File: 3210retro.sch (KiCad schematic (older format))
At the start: 25 parts, among them P101 USB_OTG, P103 LIPO, P104 DC, P106 SPEAKER, P107 HEADPHONE, P108 RUMBLE, X101 ANT_GPS, X102 ANT_GSM

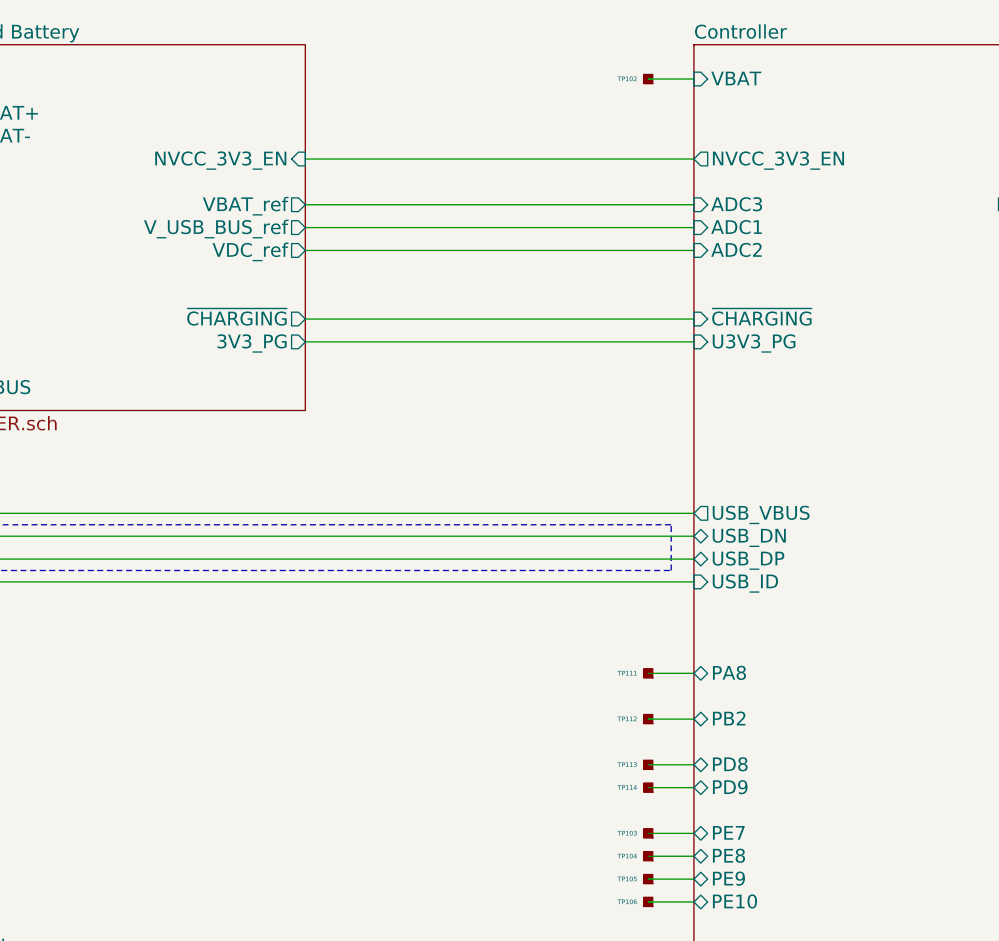
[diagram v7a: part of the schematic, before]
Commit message: finalized borad further
placed more GND vias
make 4V_BST switchable
connect GND and GNDREF through resistor
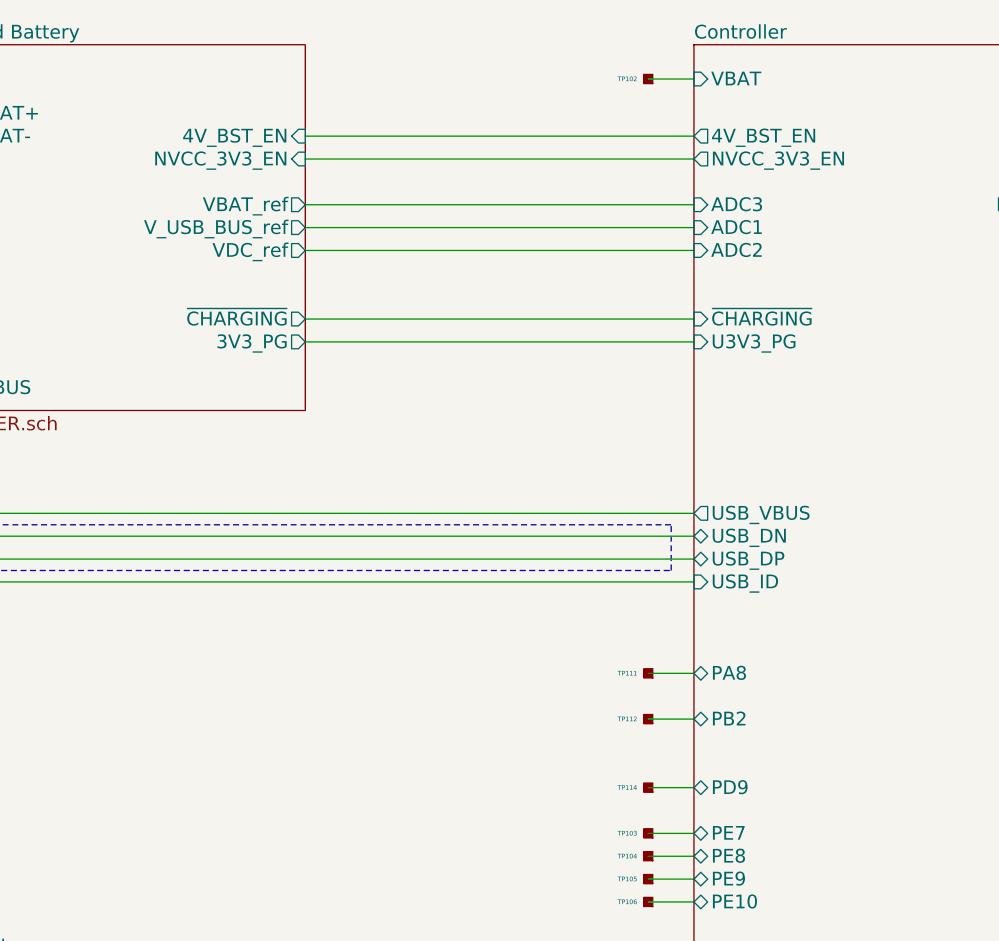
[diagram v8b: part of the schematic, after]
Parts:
- removed TP113: TP, NokiaRetroFit:TP, symbol TP
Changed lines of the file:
@@
 F11 "NVCC_3V3_EN" I R 3950 2050 60
 F12 "3V3_PG" O R 3950 2850 60
+F13 "4V_BST_EN" I R 3950 1950 60
 $EndSheet
 $Sheet
@@
 F68 "PE10" B L 5650 5300 60
 F69 "USB_DN" B L 5650 3700 60
-F70 "PD8" B L 5650 4700 60
-F71 "PD9" B L 5650 4800 60
-F72 "PB2" B L 5650 4500 60
-F73 "PA8" B L 5650 4300 60
-F74 "AUDIO_RESET" O R 7650 4350 60
+F70 "PD9" B L 5650 4800 60
+F71 "PB2" B L 5650 4500 60
+F72 "PA8" B L 5650 4300 60
+F73 "AUDIO_RESET" O R 7650 4350 60
+F74 "4V_BST_EN" O L 5650 1950 60
 $EndSheet
 $Comp
@@
 $EndComp
 $Comp
-L TP TP113
-U 1 1 59BBF2A8
-P 5450 4700
-F 0 "TP113" H 5498 4700 20  0000 L CNN
-F 1 "TP" H 5450 4650 60  0001 C CNN
-F 2 "NokiaRetroFit:TP" H 5450 4700 60  0001 C CNN
-F 3 "" H 5450 4700 60  0000 C CNN
-	1    5450 4700
-	-1   0    0    1
-$EndComp
-$Comp
 L TP TP111
 U 1 1 59BBF2AE
@@
 Wire Wire Line
 	5450 4300 5650 4300
-Wire Wire Line
-	5650 4700 5450 4700
 Wire Wire Line
 	5450 4800 5650 4800
@@
 EndData
 $EndBitmap
+Wire Wire Line
+	5650 1950 3950 1950
 $EndSCHEMATC
